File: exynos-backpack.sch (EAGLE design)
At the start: 50 parts, among them IC1 MIC5335-SPYMT, IC2 TXS0108ERGY, IC3 LTC4352DD, IC4 LTC4352DD, IC5 LTC4352DD, Q1 SI7234DP, Q2 SI7234DP, Q3 SI7234DP

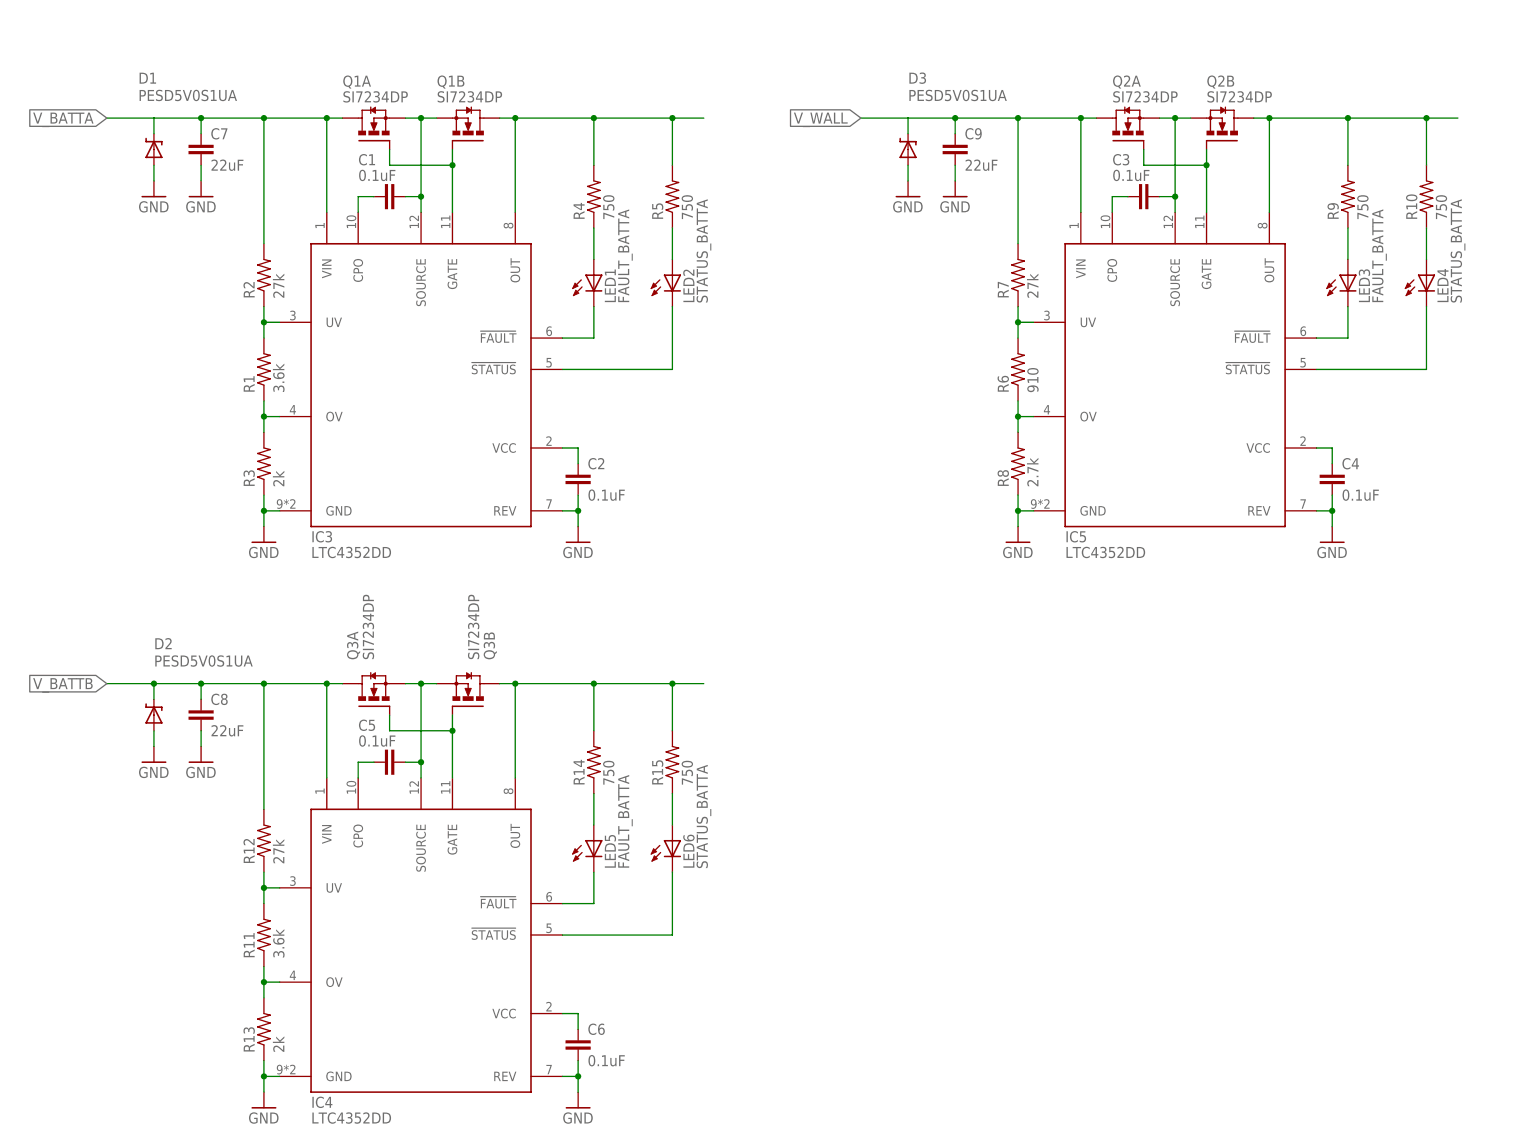
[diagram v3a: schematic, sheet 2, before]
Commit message: Add boost converter
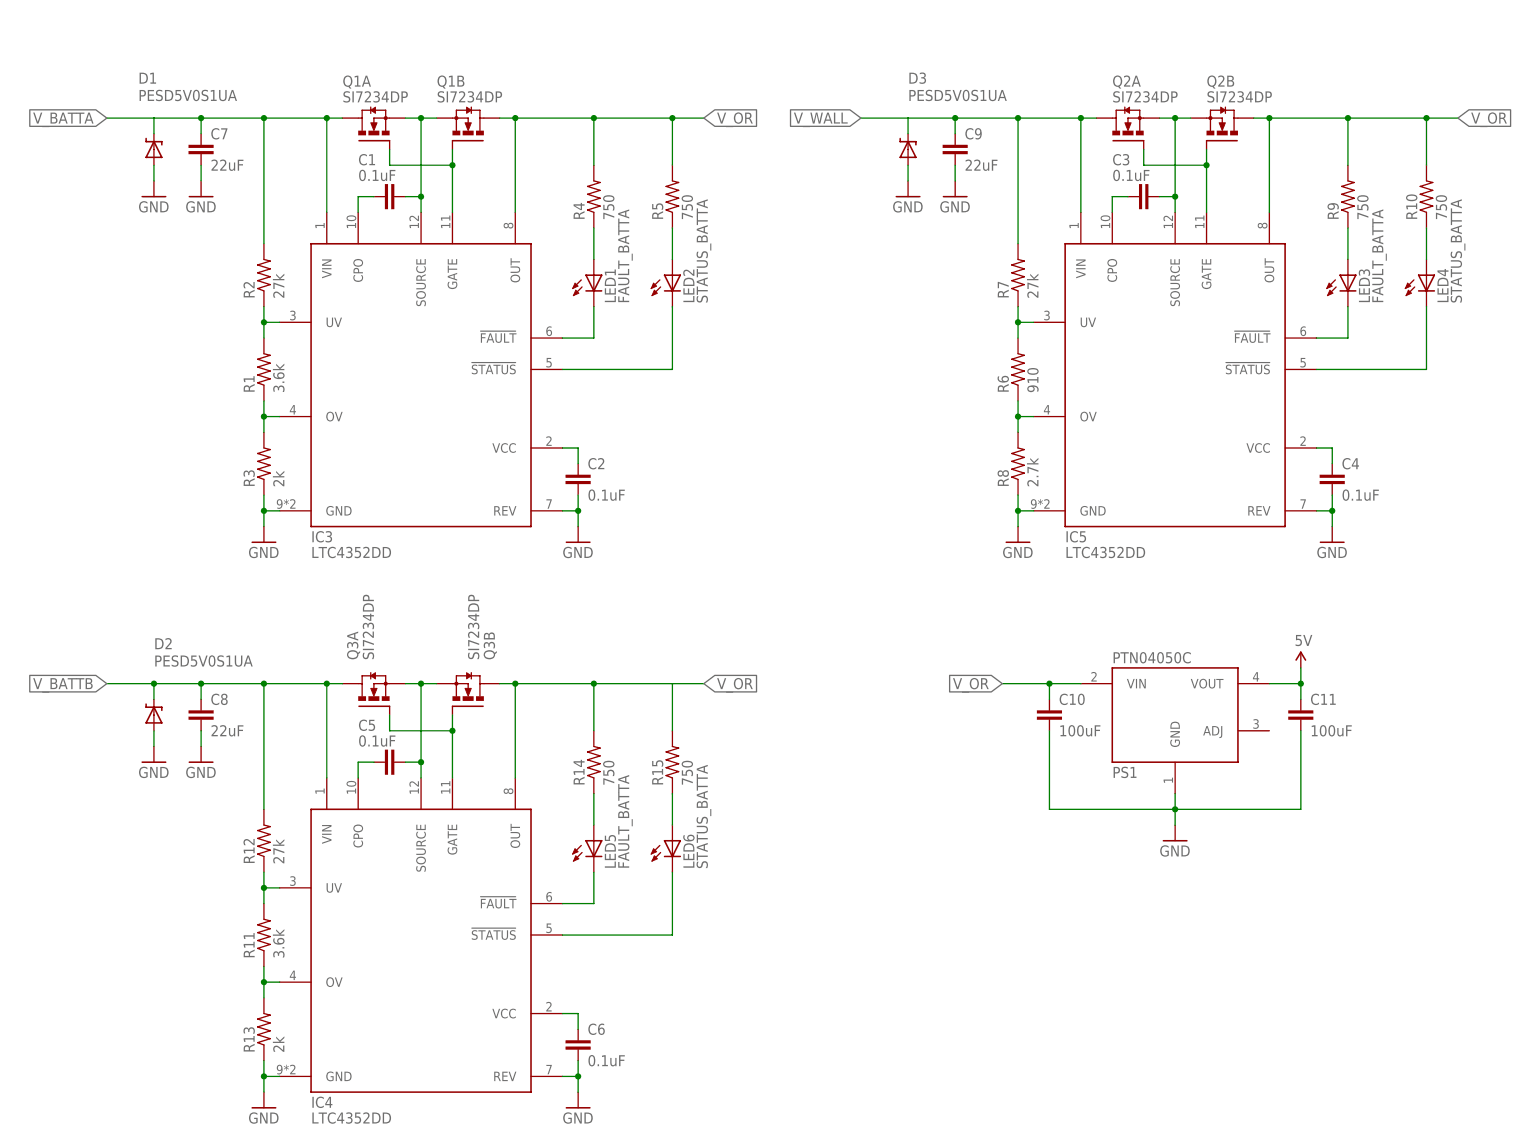
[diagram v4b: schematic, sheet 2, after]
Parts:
- added C10, C11: 100uF, biomimetic:CAP1210
- added PS1: PTN04050C, biomimetic:PTN04050C
- C7, C8, C9: device biomimetic:CAP0402-CAP -> biomimetic:CAP0603-CAP
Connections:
- removed net N$17: IC5.OUT, Q2B.D, R10.2, R9.2
- removed net N$29: IC4.OUT, Q3B.D, R14.2, R15.2
- removed net N$5: IC3.OUT, Q1B.D, R4.2, R5.2
- new net 5V: C11.1, PS1.VOUT
- new net V_OR: C10.1, IC3.OUT, IC4.OUT, IC5.OUT, PS1.VIN, Q1B.D, Q2B.D, Q3B.D, R10.2, R14.2, R15.2, R4.2, R5.2, R9.2
- net GND: now also C10.2, C11.2, PS1.GND
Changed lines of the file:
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@@
 <part name="GND8" library="biomimetic" deviceset="GND" device=""/>
 <part name="GND12" library="biomimetic" deviceset="GND" device=""/>
-<part name="C7" library="biomimetic" deviceset="CAP" device="0402-CAP" value="22uF"/>
+<part name="C7" library="biomimetic" deviceset="CAP" device="0603-CAP" value="22uF"/>
 <part name="GND13" library="biomimetic" deviceset="GND" device=""/>
-<part name="C8" library="biomimetic" deviceset="CAP" device="0402-CAP" value="22uF"/>
-<part name="C9" library="biomimetic" deviceset="CAP" device="0402-CAP" value="22uF"/>
+<part name="C8" library="biomimetic" deviceset="CAP" device="0603-CAP" value="22uF"/>
+<part name="C9" library="biomimetic" deviceset="CAP" device="0603-CAP" value="22uF"/>
 <part name="GND14" library="biomimetic" deviceset="GND" device=""/>
 <part name="GND19" library="biomimetic" deviceset="GND" device=""/>
@@
 <part name="GND21" library="biomimetic" deviceset="GND" device=""/>
 <part name="GND22" library="biomimetic" deviceset="GND" device=""/>
+<part name="PS1" library="biomimetic" deviceset="PTN04050C" device=""/>
+<part name="U$1" library="biomimetic" deviceset="5V" device=""/>
+<part name="C10" library="biomimetic" deviceset="CAP" device="1210" value="100uF"/>
+<part name="C11" library="biomimetic" deviceset="CAP" device="1210" value="100uF"/>
+<part name="GND23" library="biomimetic" deviceset="GND" device=""/>
 </parts>
 <sheets>
@@
 <instance part="GND21" gate="1" x="22.86" y="60.96"/>
 <instance part="GND22" gate="1" x="144.78" y="152.4"/>
+<instance part="PS1" gate="G$1" x="187.96" y="68.58"/>
+<instance part="U$1" gate="G$1" x="208.28" y="76.2"/>
+<instance part="C10" gate="G$1" x="167.64" y="68.58"/>
+<instance part="C11" gate="G$1" x="208.28" y="68.58"/>
+<instance part="GND23" gate="1" x="187.96" y="48.26"/>
 </instances>
 <busses>
@@
 </segment>
 </net>
-<net name="N$5" class="0">
+<net name="V_OR" class="0">
 <segment>
 <pinref part="Q1" gate="B" pin="D"/>
@@
 <junction x="93.98" y="165.1"/>
 <junction x="106.68" y="165.1"/>
+<label x="111.76" y="165.1" size="1.778" layer="95" xref="yes"/>
+</segment>
+<segment>
+<pinref part="Q3" gate="B" pin="D"/>
+<wire x1="78.74" y1="73.66" x2="81.28" y2="73.66" width="0.1524" layer="91"/>
+<wire x1="81.28" y1="73.66" x2="93.98" y2="73.66" width="0.1524" layer="91"/>
+<pinref part="IC4" gate="G$1" pin="OUT"/>
+<wire x1="93.98" y1="73.66" x2="106.68" y2="73.66" width="0.1524" layer="91"/>
+<wire x1="81.28" y1="58.42" x2="81.28" y2="73.66" width="0.1524" layer="91"/>
+<junction x="81.28" y="73.66"/>
+<pinref part="R14" gate="G$1" pin="2"/>
+<wire x1="93.98" y1="66.04" x2="93.98" y2="73.66" width="0.1524" layer="91"/>
+<pinref part="R15" gate="G$1" pin="2"/>
+<wire x1="106.68" y1="66.04" x2="106.68" y2="73.66" width="0.1524" layer="91"/>
+<junction x="93.98" y="73.66"/>
+<wire x1="106.68" y1="73.66" x2="111.76" y2="73.66" width="0.1524" layer="91"/>
+<label x="111.76" y="73.66" size="1.778" layer="95" xref="yes"/>
+</segment>
+<segment>
+<pinref part="Q2" gate="B" pin="D"/>
+<wire x1="200.66" y1="165.1" x2="203.2" y2="165.1" width="0.1524" layer="91"/>
+<wire x1="203.2" y1="165.1" x2="215.9" y2="165.1" width="0.1524" layer="91"/>
+<pinref part="IC5" gate="G$1" pin="OUT"/>
+<wire x1="215.9" y1="165.1" x2="228.6" y2="165.1" width="0.1524" layer="91"/>
+<wire x1="228.6" y1="165.1" x2="233.68" y2="165.1" width="0.1524" layer="91"/>
+<wire x1="203.2" y1="149.86" x2="203.2" y2="165.1" width="0.1524" layer="91"/>
+<junction x="203.2" y="165.1"/>
+<pinref part="R9" gate="G$1" pin="2"/>
+<wire x1="215.9" y1="157.48" x2="215.9" y2="165.1" width="0.1524" layer="91"/>
+<pinref part="R10" gate="G$1" pin="2"/>
+<wire x1="228.6" y1="157.48" x2="228.6" y2="165.1" width="0.1524" layer="91"/>
+<junction x="215.9" y="165.1"/>
+<junction x="228.6" y="165.1"/>
+<label x="233.68" y="165.1" size="1.778" layer="95" xref="yes"/>
+</segment>
+<segment>
+<pinref part="PS1" gate="G$1" pin="VIN"/>
+<wire x1="172.72" y1="73.66" x2="167.64" y2="73.66" width="0.1524" layer="91"/>
+<label x="160.02" y="73.66" size="1.778" layer="95" rot="R180" xref="yes"/>
+<pinref part="C10" gate="G$1" pin="1"/>
+<wire x1="167.64" y1="73.66" x2="160.02" y2="73.66" width="0.1524" layer="91"/>
+<wire x1="167.64" y1="71.12" x2="167.64" y2="73.66" width="0.1524" layer="91"/>
+<junction x="167.64" y="73.66"/>
 </segment>
 </net>
@@
 <pinref part="D3" gate="G$1" pin="A"/>
 <wire x1="144.78" y1="154.94" x2="144.78" y2="157.48" width="0.1524" layer="91"/>
+</segment>
+<segment>
+<pinref part="PS1" gate="G$1" pin="GND"/>
+<pinref part="GND23" gate="1" pin="GND"/>
+<wire x1="187.96" y1="55.88" x2="187.96" y2="53.34" width="0.1524" layer="91"/>
+<pinref part="C10" gate="G$1" pin="2"/>
+<wire x1="187.96" y1="53.34" x2="187.96" y2="50.8" width="0.1524" layer="91"/>
+<wire x1="167.64" y1="66.04" x2="167.64" y2="53.34" width="0.1524" layer="91"/>
+<wire x1="167.64" y1="53.34" x2="187.96" y2="53.34" width="0.1524" layer="91"/>
+<pinref part="C11" gate="G$1" pin="2"/>
+<wire x1="208.28" y1="66.04" x2="208.28" y2="53.34" width="0.1524" layer="91"/>
+<wire x1="208.28" y1="53.34" x2="187.96" y2="53.34" width="0.1524" layer="91"/>
+<junction x="187.96" y="53.34"/>
 </segment>
 </net>
@@
 <pinref part="D3" gate="G$1" pin="C"/>
 <wire x1="144.78" y1="162.56" x2="144.78" y2="165.1" width="0.1524" layer="91"/>
-</segment>
-</net>
-<net name="N$17" class="0">
-<segment>
-<pinref part="Q2" gate="B" pin="D"/>
-<wire x1="200.66" y1="165.1" x2="203.2" y2="165.1" width="0.1524" layer="91"/>
-<wire x1="203.2" y1="165.1" x2="215.9" y2="165.1" width="0.1524" layer="91"/>
-<pinref part="IC5" gate="G$1" pin="OUT"/>
-<wire x1="215.9" y1="165.1" x2="228.6" y2="165.1" width="0.1524" layer="91"/>
-<wire x1="228.6" y1="165.1" x2="233.68" y2="165.1" width="0.1524" layer="91"/>
-<wire x1="203.2" y1="149.86" x2="203.2" y2="165.1" width="0.1524" layer="91"/>
-<junction x="203.2" y="165.1"/>
-<pinref part="R9" gate="G$1" pin="2"/>
-<wire x1="215.9" y1="157.48" x2="215.9" y2="165.1" width="0.1524" layer="91"/>
-<pinref part="R10" gate="G$1" pin="2"/>
-<wire x1="228.6" y1="157.48" x2="228.6" y2="165.1" width="0.1524" layer="91"/>
-<junction x="215.9" y="165.1"/>
-<junction x="228.6" y="165.1"/>
 </segment>
 </net>
@@
 </segment>
 </net>
-<net name="N$29" class="0">
-<segment>
-<pinref part="Q3" gate="B" pin="D"/>
-<wire x1="78.74" y1="73.66" x2="81.28" y2="73.66" width="0.1524" layer="91"/>
-<wire x1="81.28" y1="73.66" x2="93.98" y2="73.66" width="0.1524" layer="91"/>
-<pinref part="IC4" gate="G$1" pin="OUT"/>
-<wire x1="93.98" y1="73.66" x2="106.68" y2="73.66" width="0.1524" layer="91"/>
-<wire x1="106.68" y1="73.66" x2="111.76" y2="73.66" width="0.1524" layer="91"/>
-<wire x1="81.28" y1="58.42" x2="81.28" y2="73.66" width="0.1524" layer="91"/>
-<junction x="81.28" y="73.66"/>
-<pinref part="R14" gate="G$1" pin="2"/>
-<wire x1="93.98" y1="66.04" x2="93.98" y2="73.66" width="0.1524" layer="91"/>
-<pinref part="R15" gate="G$1" pin="2"/>
-<wire x1="106.68" y1="66.04" x2="106.68" y2="73.66" width="0.1524" layer="91"/>
-<junction x="93.98" y="73.66"/>
-<junction x="106.68" y="73.66"/>
-</segment>
-</net>
 <net name="N$30" class="0">
 <segment>
@@
 </segment>
 </net>
+<net name="5V" class="0">
+<segment>
+<pinref part="U$1" gate="G$1" pin="5V"/>
+<pinref part="C11" gate="G$1" pin="1"/>
+<wire x1="208.28" y1="76.2" x2="208.28" y2="73.66" width="0.1524" layer="91"/>
+<pinref part="PS1" gate="G$1" pin="VOUT"/>
+<wire x1="208.28" y1="73.66" x2="208.28" y2="71.12" width="0.1524" layer="91"/>
+<wire x1="203.2" y1="73.66" x2="208.28" y2="73.66" width="0.1524" layer="91"/>
+<junction x="208.28" y="73.66"/>
+</segment>
+</net>

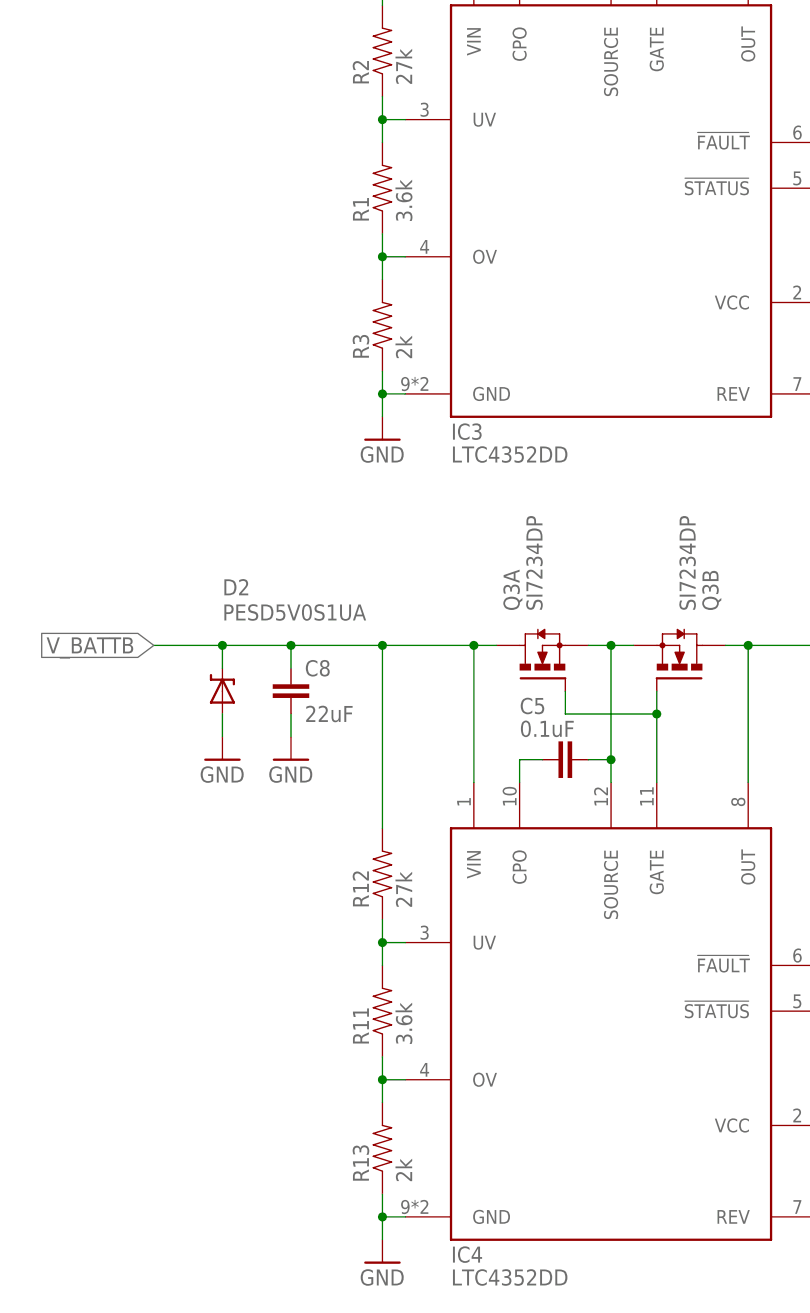
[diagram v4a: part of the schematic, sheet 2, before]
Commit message: Reduce current-limiting resistor values
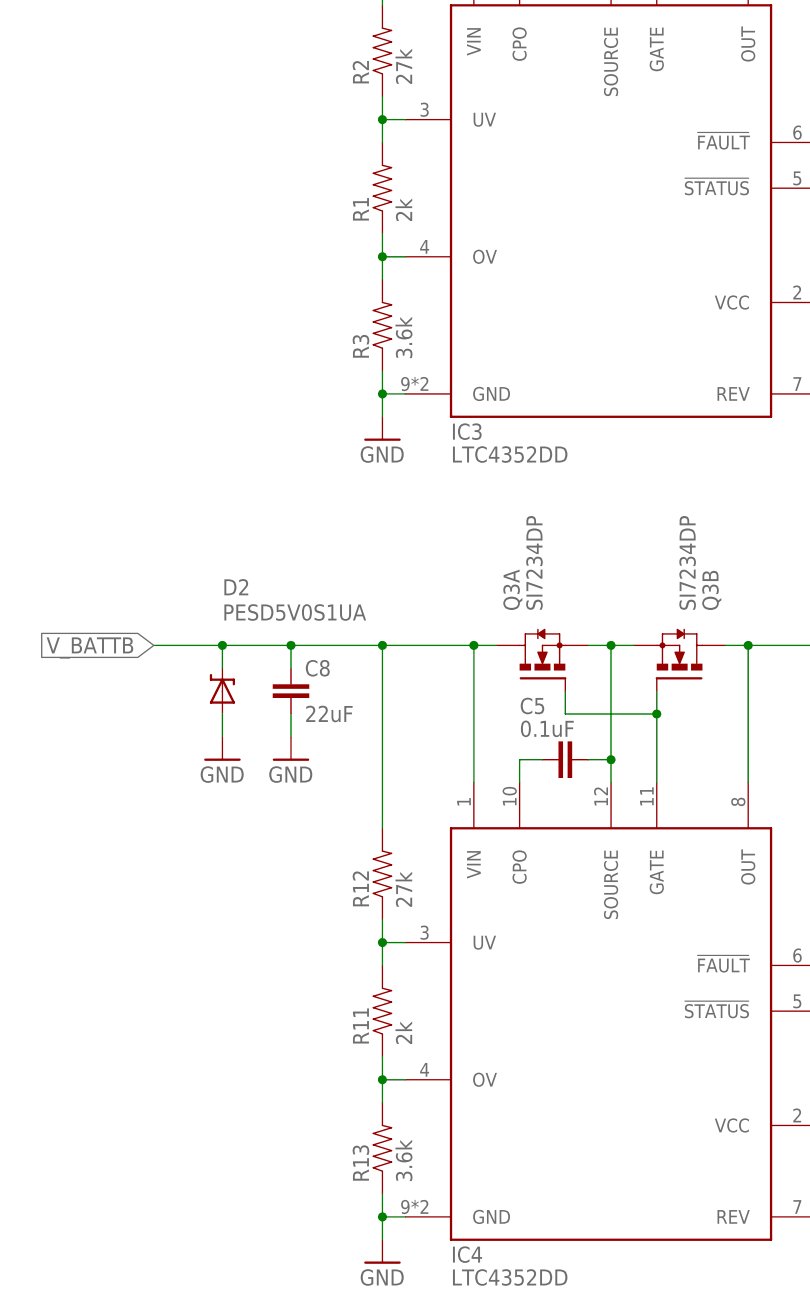
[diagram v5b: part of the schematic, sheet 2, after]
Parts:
- R1, R11: value 3.6k -> 2k
- R13, R3: value 2k -> 3.6k
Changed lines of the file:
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@@
 <part name="FRAME1" library="biomimetic" deviceset="FRAME-LETTER" device=""/>
 <part name="IC3" library="biomimetic" deviceset="LTC4352" device="DD"/>
-<part name="R1" library="biomimetic" deviceset="RESISTOR" device="0402-RES" value="3.6k"/>
+<part name="R1" library="biomimetic" deviceset="RESISTOR" device="0402-RES" value="2k"/>
 <part name="R2" library="biomimetic" deviceset="RESISTOR" device="0402-RES" value="27k"/>
-<part name="R3" library="biomimetic" deviceset="RESISTOR" device="0402-RES" value="2k"/>
+<part name="R3" library="biomimetic" deviceset="RESISTOR" device="0402-RES" value="3.6k"/>
 <part name="Q1" library="biomimetic" deviceset="SI7234DP" device=""/>
 <part name="C1" library="biomimetic" deviceset="CAP" device="0402-CAP" value="0.1uF"/>
@@
 <part name="GND7" library="biomimetic" deviceset="GND" device=""/>
 <part name="IC4" library="biomimetic" deviceset="LTC4352" device="DD"/>
-<part name="R11" library="biomimetic" deviceset="RESISTOR" device="0402-RES" value="3.6k"/>
+<part name="R11" library="biomimetic" deviceset="RESISTOR" device="0402-RES" value="2k"/>
 <part name="R12" library="biomimetic" deviceset="RESISTOR" device="0402-RES" value="27k"/>
-<part name="R13" library="biomimetic" deviceset="RESISTOR" device="0402-RES" value="2k"/>
+<part name="R13" library="biomimetic" deviceset="RESISTOR" device="0402-RES" value="3.6k"/>
 <part name="Q3" library="biomimetic" deviceset="SI7234DP" device=""/>
 <part name="C5" library="biomimetic" deviceset="CAP" device="0402-CAP" value="0.1uF"/>
